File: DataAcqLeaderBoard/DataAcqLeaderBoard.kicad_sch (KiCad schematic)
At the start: 63 parts, among them J2 USB_C_Receptacle_USB2.0_16P, J3 Conn_01x02, J4 Conn_01x02, J5 Conn_01x02, J6 Conn_01x02, J7 Conn_01x02, SW1 UP, SW2 UP, SW4 UP, SW5 UP, U1 PA1616S_GPS, U2 USBLC6-2SC6, X1 DigiXBeeRX900Micro, X2 DigiXBee3LTECat4

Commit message: First revision of schematic done
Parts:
- removed J2: USB_C_Receptacle_USB2.0_16P, symbol Connector:USB_C_Receptacle_USB2.0_16P
- removed R18, R19, R2: 470, symbol Device:R
- removed R21: 5.1k, symbol Device:R
- removed R3, R4: 10k, symbol Device:R
- removed U2: USBLC6-2SC6, Package_TO_SOT_SMD:SOT-23-6, symbol Power_Protection:USBLC6-2SC6
- added BAT1: ML414, DataAcqLeaderBoard-Footprints:BAT_2994TR, symbol DataAcqLeaderBoard-Symbols:2994TR
- added C18: 1u, Capacitor_SMD:C_0805_2012Metric, symbol Device:C
- added C6: 100u, Capacitor_SMD:C_0805_2012Metric, symbol Device:C
- added H1, H2, H3: M.3, MountingHole:MountingHole_3mm, symbol Mechanical:MountingHole
- added R13, R14: 10k, Resistor_SMD:R_0805_2012Metric, symbol Device:R
- added R7, R8: 700, Resistor_SMD:R_0805_2012Metric, symbol Device:R
- added TP1: RF_UART_RX, UTSVT_Special:TestPoint_HEX_3mmID, symbol Connector:TestPoint
- added TP2: RF_UART_TX, UTSVT_Special:TestPoint_HEX_3mmID, symbol Connector:TestPoint
- added TP3: RF_NREST, UTSVT_Special:TestPoint_HEX_3mmID, symbol Connector:TestPoint
- added TP4: LTE_UART_TX, UTSVT_Special:TestPoint_HEX_3mmID, symbol Connector:TestPoint
- added TP5: LTE_UART_RX, UTSVT_Special:TestPoint_HEX_3mmID, symbol Connector:TestPoint
- added TP6: LTE_NRESET, UTSVT_Special:TestPoint_HEX_3mmID, symbol Connector:TestPoint
- C1: renamed from C4; footprint (none) -> Capacitor_SMD:C_0805_2012Metric
- C10, C11, C12, C13, C8, C9: footprint (none) -> Capacitor_SMD:C_0805_2012Metric
- C14: renamed from C15; footprint (none) -> Capacitor_SMD:C_0805_2012Metric
- C15: renamed from C1; footprint (none) -> Capacitor_SMD:C_0805_2012Metric
- C16: renamed from C2; footprint (none) -> Capacitor_SMD:C_0805_2012Metric
- C17: renamed from C14; footprint (none) -> Capacitor_SMD:C_0805_2012Metric
- C19: renamed from C3; footprint (none) -> Capacitor_SMD:C_0805_2012Metric
- C2: renamed from C5; footprint (none) -> Capacitor_SMD:C_0805_2012Metric
- C3: renamed from C6; footprint (none) -> Capacitor_SMD:C_0805_2012Metric
- C4: renamed from C18; footprint (none) -> Capacitor_SMD:C_0805_2012Metric
- C5: renamed from C16; footprint (none) -> Capacitor_SMD:C_0805_2012Metric
- C7: value 470u -> 100u; footprint (none) -> Capacitor_SMD:C_0805_2012Metric
- D1: value LED -> RF_COM; footprint (none) -> LED_SMD:LED_0805_2012Metric; Mouser Part Number (none) -> 604-APTD2012LCGCK
- D2: value LED -> RF_MOD; footprint (none) -> LED_SMD:LED_0805_2012Metric; Mouser Part Number (none) -> 604-APTD2012LCGCK
- D3: value LED -> RF_ON; footprint (none) -> LED_SMD:LED_0805_2012Metric; Mouser Part Number (none) -> 604-APTD2012LCGCK
- D4: value LED -> RF_RSSI; footprint (none) -> LED_SMD:LED_0805_2012Metric; Mouser Part Number (none) -> 604-APTD2012LCGCK
- D5: value LED -> LTE_CONN; footprint (none) -> LED_SMD:LED_0805_2012Metric; Mouser Part Number (none) -> 604-APTD2012LCGCK
- D6: value LED -> LTE_RSSI; footprint (none) -> LED_SMD:LED_0805_2012Metric; Mouser Part Number (none) -> 604-APTD2012LCGCK
- D7: value LED -> LTE_ON; footprint (none) -> LED_SMD:LED_0805_2012Metric; Mouser Part Number (none) -> 604-APTD2012LCGCK
- D8: value LED -> !3D_FX; footprint (none) -> LED_SMD:LED_0805_2012Metric; Mouser Part Number (none) -> 604-APTD2012LCGCK
- FB1: footprint (none) -> Resistor_SMD:R_0402_1005Metric; Mouser Part Number (none) -> https://www.digikey.com/en/products/detail/pulse-electronic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
- J2: renamed from J3; value Conn_01x02 -> PER_CAN
- J3: renamed from J4; value Conn_01x02 -> PER_PWR
- J4: renamed from J5; value Conn_01x02 -> CCAN_IN
- J5: renamed from J6; value Conn_01x02 -> CCAN_OUT
- J6: renamed from J7; value Conn_01x02 -> PWR_IN
- R1: renamed from R13; footprint (none) -> Resistor_SMD:R_0805_2012Metric; Mouser Part Number (none) -> 71-CRCW080510K0FKEAC
- R10, R11, R12, R17, R9: value 470 -> 700; footprint (none) -> Resistor_SMD:R_0805_2012Metric
- R15: renamed from R16; footprint (none) -> Resistor_SMD:R_0805_2012Metric; Mouser Part Number (none) -> 71-CRCW080510K0FKEAC
- R16: renamed from R23; value 470 -> 700; footprint (none) -> Resistor_SMD:R_0805_2012Metric
- R18: renamed from R1; footprint (none) -> Resistor_SMD:R_0805_2012Metric; Mouser Part Number (none) -> 71-CRCW080510K0FKEAC
- R19: renamed from R22; value 470 -> 700; footprint (none) -> Resistor_SMD:R_0805_2012Metric
- R2: renamed from R7; footprint (none) -> Resistor_SMD:R_0805_2012Metric; Mouser Part Number (none) -> 71-CRCW080510K0FKEAC
- R20: value 5.1k -> 700; footprint (none) -> Resistor_SMD:R_0805_2012Metric
- R3: renamed from R5; footprint (none) -> Resistor_SMD:R_0805_2012Metric; Mouser Part Number (none) -> 71-CRCW080510K0FKEAC
- R4: renamed from R6; value 470 -> 700; footprint (none) -> Resistor_SMD:R_0805_2012Metric
- R5: renamed from R8; footprint (none) -> Resistor_SMD:R_0805_2012Metric; Mouser Part Number (none) -> 71-CRCW080510K0FKEAC
- R6: renamed from R24; value 470 -> 700; footprint (none) -> Resistor_SMD:R_0805_2012Metric
- SW1: renamed from SW5; value UP -> RF_RESET; footprint (none) -> Button_Switch_SMD:SW_SPST_B3SL-1002P
- SW2: value UP -> RF_COM; footprint (none) -> Button_Switch_SMD:SW_SPST_B3SL-1002P
- SW3: renamed from SW4; value UP -> LTE_RESET; footprint (none) -> Button_Switch_SMD:SW_SPST_B3SL-1002P
- SW4: renamed from SW1; value UP -> GPS_RESET; footprint (none) -> Button_Switch_SMD:SW_SPST_B3SL-1002P
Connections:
- net USBC_CC1 is gone; now on net GPS_3D_Fix: R20.1
- net +3.3V: now also C6.1, R13.1, R14.1
- net GND: now also D1.1 (K), D2.1 (K), D3.1 (K), D4.1 (K), D5.1 (K), D6.1 (K), D7.1 (K), D8.1 (K), BAT1.N, C18.2, C6.2; no longer R10.2, R11.2, R12.2, R17.2, R20.2, R9.2
- net GPS_3D_Fix: no longer D1.2 (A)
- net GPS_CoinBattery_Supply: now also BAT1.P1, BAT1.P2, C18.1
- net LTE_NRESET: now also TP6.1
- net LTE_STATUS_CONN: now also R11.1; no longer D8.2 (A)
- net LTE_STATUS_ON: now also R17.1; no longer D7.2 (A)
- net LTE_STATUS_RSSI: now also R12.1; no longer D6.2 (A)
- net LTE_UART_RX: now also TP5.1
- net LTE_UART_TX: now also TP4.1
- net RF_NRESET: now also TP3.1
- net RF_STATUS_AWAKE: now also R9.1; no longer D4.2 (A)
- net RF_STATUS_COMMISION: now also R7.1; no longer D2.2 (A)
- net RF_STATUS_MODULE: now also R8.1; no longer D3.2 (A)
- net RF_STATUS_RSSI: now also R10.1; no longer D5.2 (A)
- net RF_UART_RX: now also TP1.1
- net RF_UART_TX: now also TP2.1
- net LTE_USB_D+: no longer names the net of X2.7 (PWM1/DIO11/USB_D+/I2C_SDA)
- net LTE_USB_D+: now also R13.2
- net LTE_USB_D-: no longer names the net of X2.8 (USB_D-)
- net LTE_USB_D-: now also R14.2
- new net: D5.2 (A), R11.2
- new net: D3.2 (A), R9.2
- new net: D7.2 (A), R17.2
- new net: D1.2 (A), R7.2
- new net: D8.2 (A), R20.2
- new net: D2.2 (A), R8.2
- new net: D6.2 (A), R12.2
- new net: D4.2 (A), R10.2
- no-connect marks 23 -> 21
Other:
- note added: "Mouting"
- note added: "Pin 20 not used in this version of LTE module"
- note added: "R=(Vs-Vf)/If = (3.3-1.9)/2mA = 700"
- note removed: "Awake"
- note removed: "CONN"
- note removed: "Commision"
- note removed: "Module"
- note removed: "Neg 3D Fix"
- note removed: "ON"
- note removed: "RSSI"
- company: (none) -> Longhorn Racing Solar
- title: (none) -> DataAcq-LeaderPCB
- moved on the sheet: C10, C11, C12, C13, C14, C8, C9, R15, R16, R3, R5, SW3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

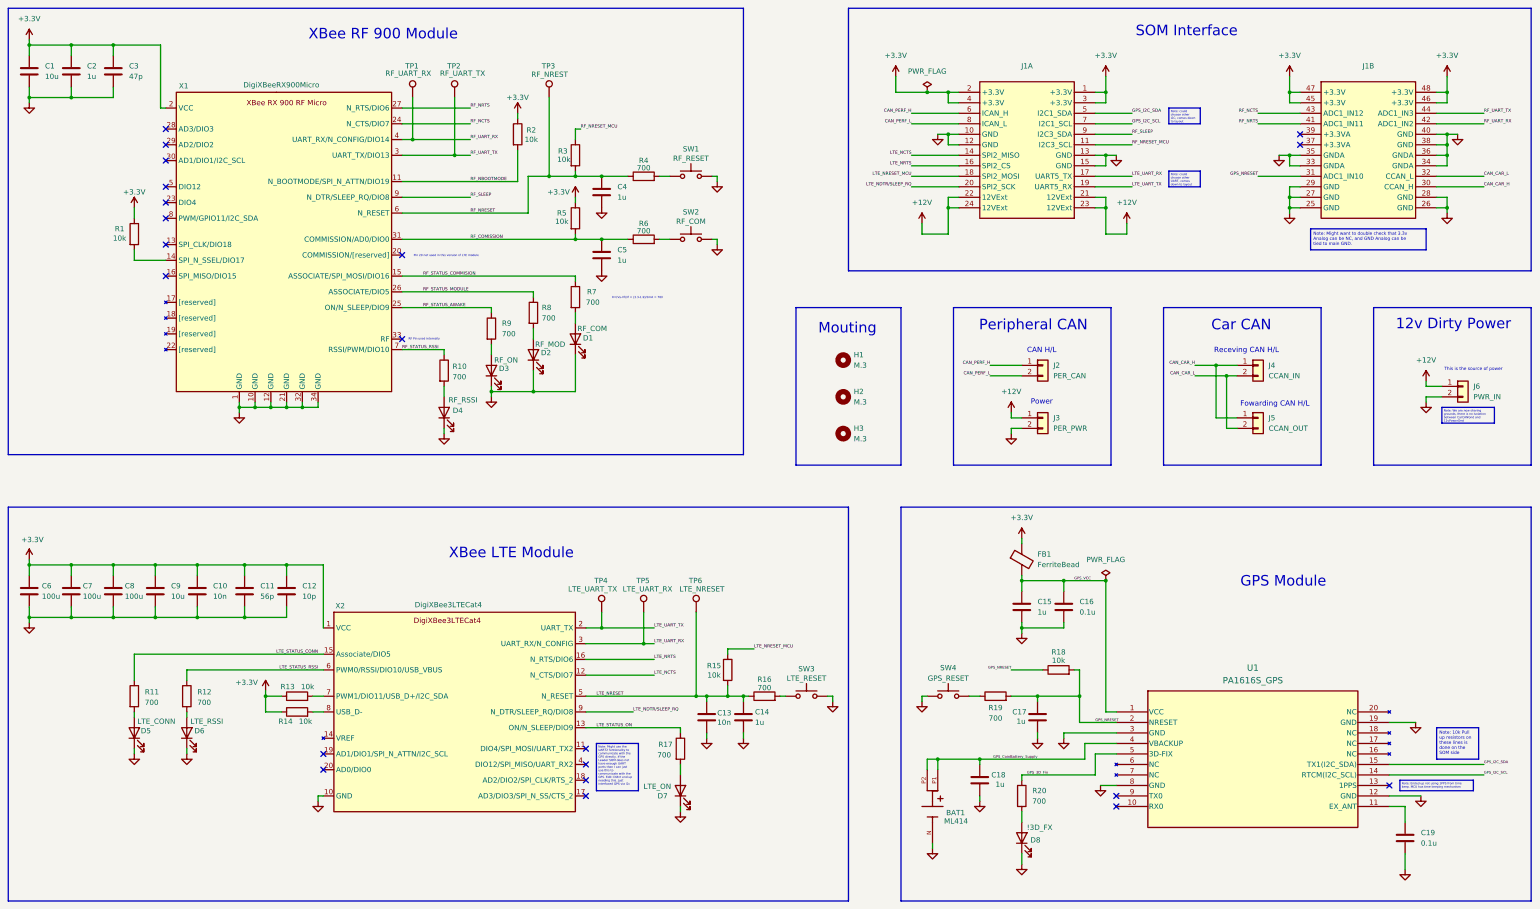
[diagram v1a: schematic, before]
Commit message: Completed first draft of layout
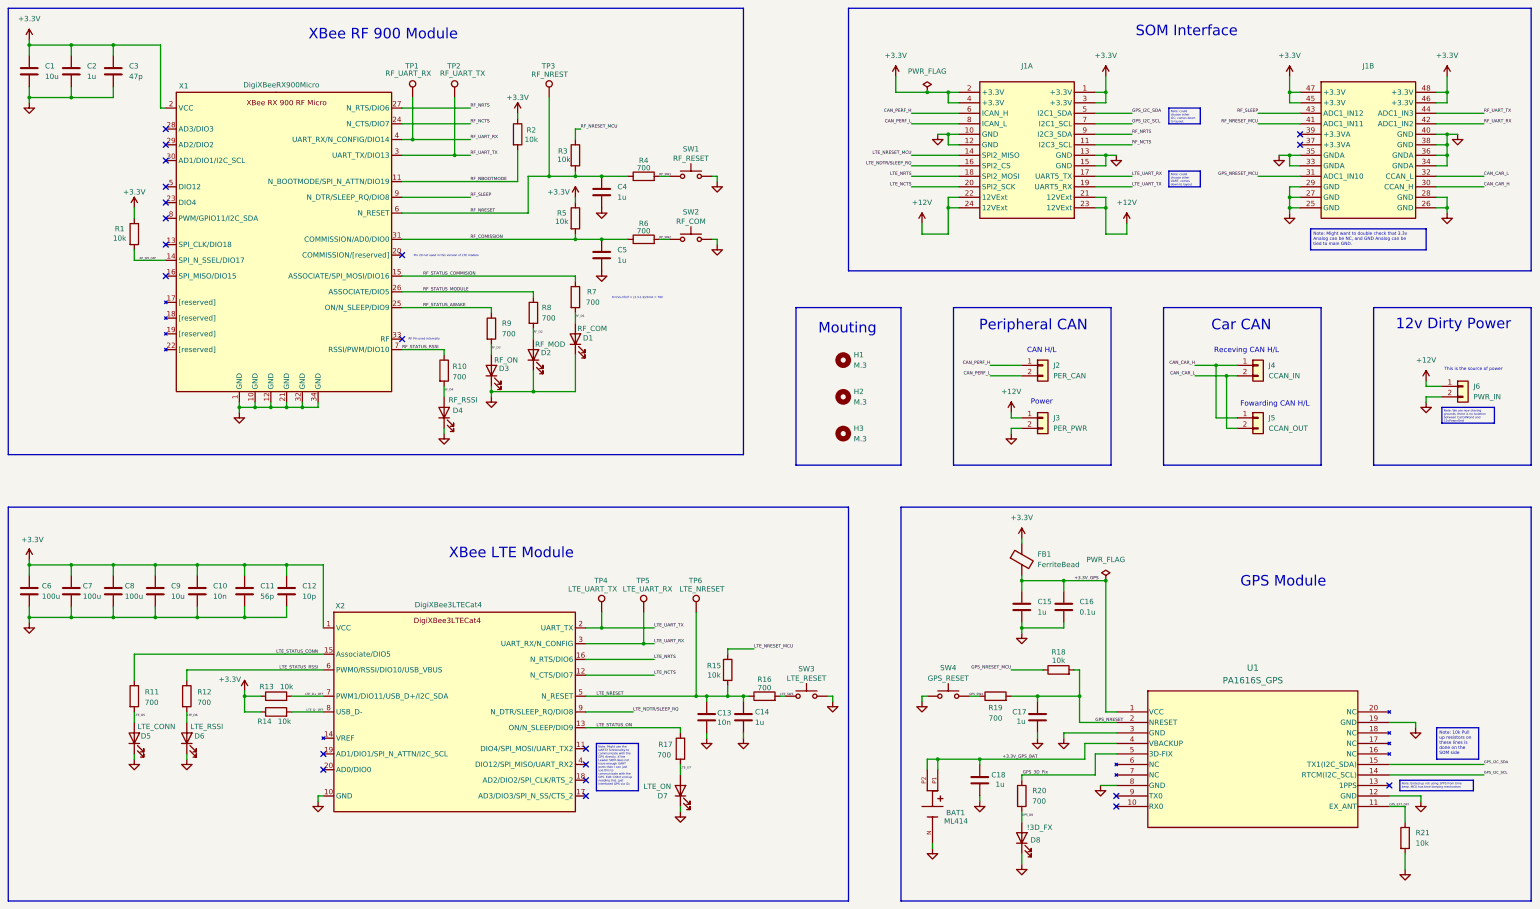
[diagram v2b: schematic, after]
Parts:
- removed C19: 0.1u, Capacitor_SMD:C_0805_2012Metric, symbol Device:C
- added R21: 10k, Resistor_SMD:R_0805_2012Metric, symbol Device:R
- J2, J3, J4, J5, J6: footprint Connector_PinHeader_2.00mm:PinHeader_1x02_P2.00mm_Vertical -> DataAcqLeaderBoard-Footprints:CONN_SD-43650-006_02_MOL
- SW1: Mouser Part Number (none) -> 653-B3SL-1002P
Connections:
- net GND: now also R21.2
- net GPS_NRESET: no longer J1.31 (ADC1_IN10), R18.1
- net LTE_NCTS: now also J1.20 (SPI2_SCK); no longer J1.14 (SPI2_MISO)
- net LTE_NDTR/SLEEP_RQ: now also J1.16 (SPI2_CS); no longer J1.20 (SPI2_SCK)
- net LTE_NRESET_MCU: now also J1.14 (SPI2_MISO); no longer J1.18 (SPI2_MOSI)
- net LTE_NRTS: now also J1.18 (SPI2_MOSI); no longer J1.16 (SPI2_CS)
- net RF_NCTS: now also J1.11 (I2C3_SCL); no longer J1.43 (ADC1_IN12)
- net RF_NRESET_MCU: now also J1.41 (ADC1_IN11); no longer J1.11 (I2C3_SCL)
- net RF_NRTS: now also J1.9 (I2C3_SDA); no longer J1.41 (ADC1_IN11)
- net RF_SLEEP: now also J1.43 (ADC1_IN12); no longer J1.9 (I2C3_SDA)
- net LTE_D+_OFF: now reaches R13.2, X2.7 (PWM1/DIO11/USB_D+/I2C_SDA)
- net LTE_D5: now reaches D5.2 (A), R11.2
- net RF_D3: now reaches D3.2 (A), R9.2
- net LTE_D7: now reaches D7.2 (A), R17.2
- net GPS_EXT_OFF: now reaches U1.11 (EX_ANT)
- net GPS_EXT_OFF: now also R21.1
- net RF_SW2: now reaches R6.2, SW2.1
- net RF_D1: now reaches D1.2 (A), R7.2
- net GPS_D8: now reaches D8.2 (A), R20.2
- net RF_D2: now reaches D2.2 (A), R8.2
- net LTE_SW3: now reaches R16.2, SW3.1
- net RF_SPI_OFF: now reaches R1.2, X1.14 (SPI_N_SSEL/DIO17)
- net RF_SW1: now reaches R4.2, SW1.1
- net LTE_D-_OFF: now reaches R14.2, X2.8 (USB_D-)
- net GPS_SW4: now reaches R19.1, SW4.2
- net LTE_D6: now reaches D6.2 (A), R12.2
- net RF_D4: now reaches D4.2 (A), R10.2
- net GPS_CoinBattery_Supply renamed +3.3V_GPS_BAT
- net GPS_VCC renamed +3.3V_GPS
- new net GPS_NRESET_MCU: J1.31 (ADC1_IN10), R18.1
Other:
- moved on the sheet: D5, D6, R13, R14

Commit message: Updated Schematic, finished first rev of Layout
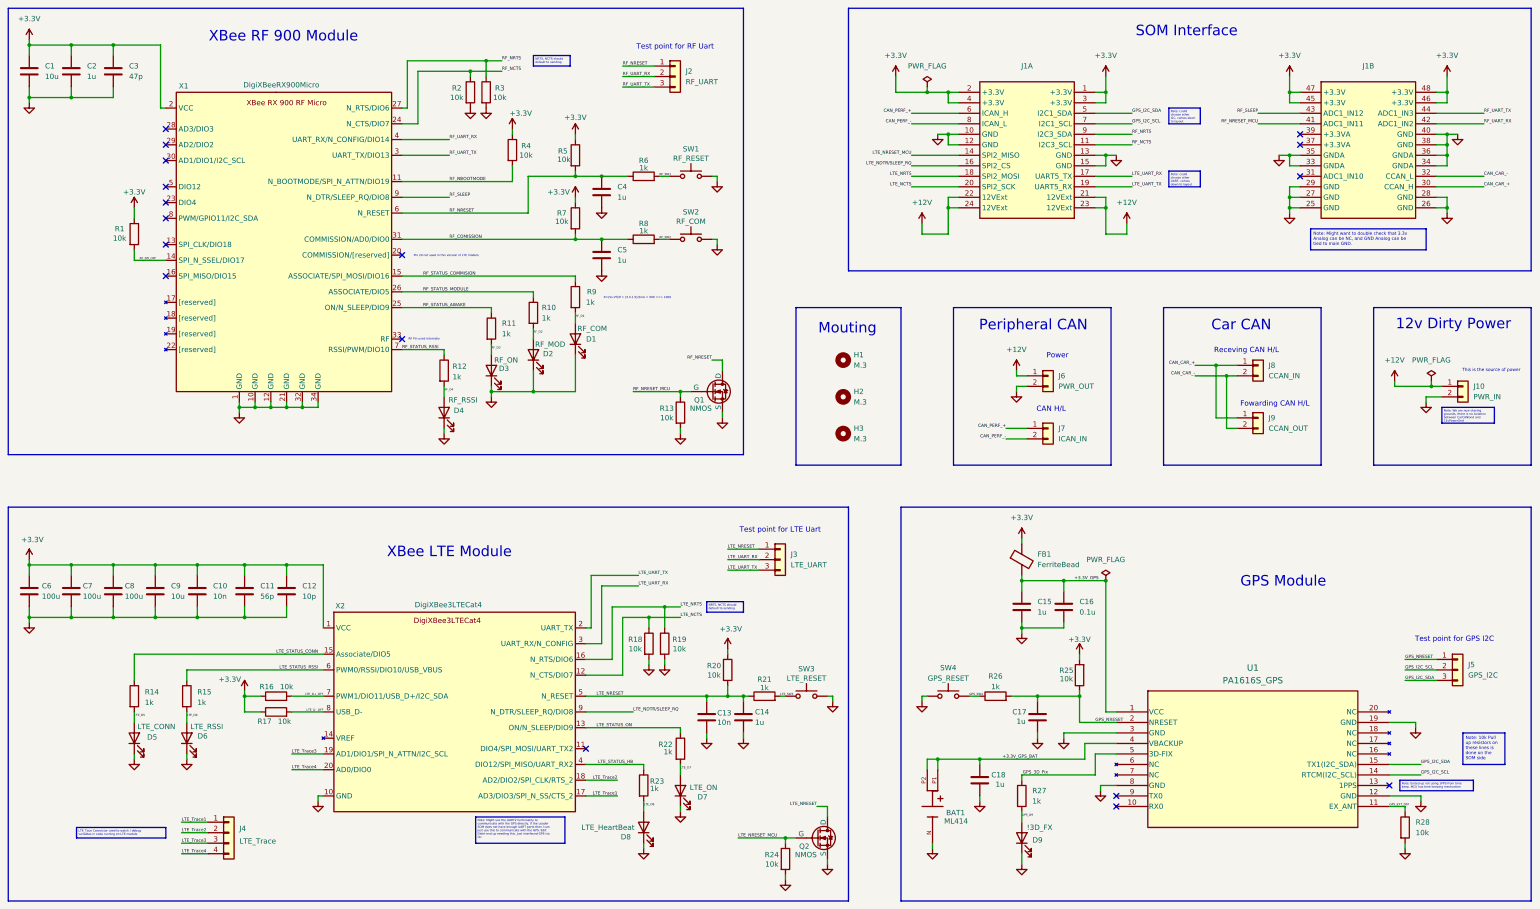
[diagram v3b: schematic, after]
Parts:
- removed J2: PER_CAN, DataAcqLeaderBoard-Footprints:CONN_SD-43650-006_02_MOL, symbol Connector_Generic:Conn_01x02
- removed J3: PER_PWR, DataAcqLeaderBoard-Footprints:CONN_SD-43650-006_02_MOL, symbol Connector_Generic:Conn_01x02
- removed TP1: RF_UART_RX, UTSVT_Special:TestPoint_HEX_3mmID, symbol Connector:TestPoint
- removed TP2: RF_UART_TX, UTSVT_Special:TestPoint_HEX_3mmID, symbol Connector:TestPoint
- removed TP3: RF_NREST, UTSVT_Special:TestPoint_HEX_3mmID, symbol Connector:TestPoint
- removed TP4: LTE_UART_TX, UTSVT_Special:TestPoint_HEX_3mmID, symbol Connector:TestPoint
- removed TP5: LTE_UART_RX, UTSVT_Special:TestPoint_HEX_3mmID, symbol Connector:TestPoint
- removed TP6: LTE_NRESET, UTSVT_Special:TestPoint_HEX_3mmID, symbol Connector:TestPoint
- added D8: LTE_HeartBeat, LED_SMD:LED_0805_2012Metric, symbol Device:LED
- added J2: RF_UART, Connector_PinHeader_2.54mm:PinHeader_1x03_P2.54mm_Vertical, symbol Connector_Generic:Conn_01x03
- added J3: LTE_UART, Connector_PinHeader_2.54mm:PinHeader_1x03_P2.54mm_Vertical, symbol Connector_Generic:Conn_01x03
- added J4: LTE_Trace, Connector_PinHeader_2.54mm:PinHeader_1x04_P2.54mm_Vertical, symbol Connector_Generic:Conn_01x04
- added J5: GPS_I2C, Connector_PinHeader_2.54mm:PinHeader_1x03_P2.54mm_Vertical, symbol Connector_Generic:Conn_01x03
- added J6: PWR_OUT, DataAcqLeaderBoard-Footprints:CONN_SD-43650-006_02_MOL, symbol Connector_Generic:Conn_01x02
- added J7: ICAN_IN, DataAcqLeaderBoard-Footprints:CONN_SD-43650-006_02_MOL, symbol Connector_Generic:Conn_01x02
- added Q1, Q2: NMOS, Package_TO_SOT_SMD:SOT-23-3, symbol Simulation_SPICE:NMOS
- added R13, R18, R19, R2, R24, R3: 10k, Resistor_SMD:R_0805_2012Metric, symbol Device:R
- added R23: 1k, Resistor_SMD:R_0805_2012Metric, symbol Device:R
- R10: renamed from R8; value 700 -> 1k
- R11: renamed from R9; value 700 -> 1k
- R12: renamed from R10; value 700 -> 1k
- R14: renamed from R11; value 700 -> 1k
- R15: renamed from R12; value 700 -> 1k
- R21: renamed from R16; value 700 -> 1k
- R22: renamed from R17; value 700 -> 1k
- R26: renamed from R19; value 700 -> 1k
- R27: renamed from R20; value 700 -> 1k
- R6: renamed from R4; value 700 -> 1k
- R8: renamed from R6; value 700 -> 1k
- R9: renamed from R7; value 700 -> 1k
- U1: Mouser Part Number (none) -> https://www.adafruit.com/product/790?gad_source=1&gclid=Cj0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
- renumbered D8 to D9, J6 to J10, J4 to J8, J5 to J9, R13 to R16, R14 to R17, R15 to R20, R18 to R25, R21 to R28, R2 to R4, R3 to R5, R5 to R7
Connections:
- net +12V: now also J6.1 (Pin_1)
- net +3.3V: now also R20.1, R25.2, R5.1
- net GND: now also D8.1 (K), J6.2 (Pin_2), Q1.3 (S), Q2.3 (S), R13.2, R18.2, R19.2, R2.2, R24.2, R3.2
- net GPS_I2C_SCL: now also J5.2 (Pin_2)
- net GPS_I2C_SDA: now also J5.3 (Pin_3)
- net GPS_NRESET: now also R25.1, J5.1 (Pin_1); no longer R25.2
- net LTE_NCTS: now also R18.1
- net LTE_NRESET: now also J3.1 (Pin_1), Q2.1 (D)
- net LTE_NRESET_MCU: now also Q2.2 (G), R24.1; no longer R20.1
- net LTE_NRTS: now also R19.1
- net LTE_UART_RX: now also J3.2 (Pin_2)
- net LTE_UART_TX: now also J3.3 (Pin_3)
- net RF_NCTS: now also R2.1
- net RF_NRESET: now also J2.1 (Pin_1), Q1.1 (D)
- net RF_NRESET_MCU: now also Q1.2 (G), R13.1; no longer R5.1
- net RF_NRTS: now also R3.1
- net RF_UART_RX: now also J2.2 (Pin_2)
- net RF_UART_TX: now also J2.3 (Pin_3)
- net LTE_Trace1: now reaches X2.17 (AD3/DIO3/SPI_N_SS/CTS_2)
- net LTE_Trace1: now also J4.1 (Pin_1)
- net LTE_Trace2: now reaches X2.18 (AD2/DIO2/SPI_CLK/RTS_2)
- net LTE_Trace2: now also J4.2 (Pin_2)
- net LTE_Trace3: now reaches X2.19 (AD1/DIO1/SPI_N_ATTN/I2C_SCL)
- net LTE_Trace3: now also J4.3 (Pin_3)
- net LTE_Trace4: now reaches X2.20 (AD0/DIO0)
- net LTE_Trace4: now also J4.4 (Pin_4)
- net LTE_STATUS_HB: now reaches X2.4 (DIO12/SPI_MISO/UART_RX2)
- net LTE_STATUS_HB: now also R23.1
- net CAN_CAR_H renamed CAN_CAR_+
- net CAN_CAR_L renamed CAN_CAR_-
- net CAN_PERF_H renamed CAN_PERF_+
- net CAN_PERF_+: now also J7.1 (Pin_1)
- net CAN_PERF_L renamed CAN_PERF_-
- net CAN_PERF_-: now also J7.2 (Pin_2)
- net GPS_D8 renamed GPS_D9
- net GPS_NRESET_MCU: no longer names the net of J1.31 (ADC1_IN10)
- net GPS_NRESET_MCU: no longer R25.1
- new net LTE_D8: D8.2 (A), R23.2
- no-connect marks 21 -> 17
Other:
- note added: "R=(Vs-Vf)/If = (3.3-1.5)/2mA = 900 ==> 1000"
- note added: "Test point for GPS I2C"
- note added: "Test point for LTE Uart"
- note added: "Test point for RF Uart"
- note removed: "R=(Vs-Vf)/If = (3.3-1.9)/2mA = 700"
- moved on the sheet: R25, R28, R4
